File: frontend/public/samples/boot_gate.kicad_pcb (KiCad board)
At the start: 3 parts, among them Q1 2N7002, U1 ATmega328P

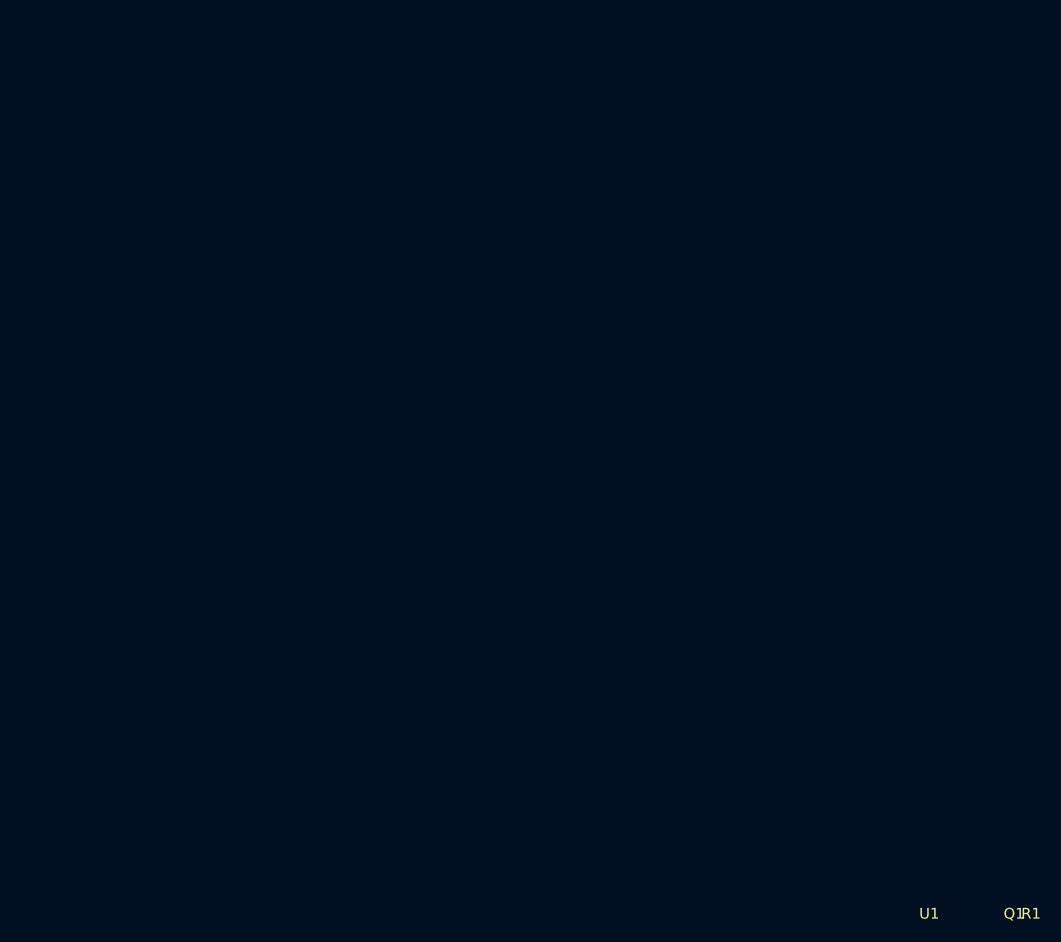
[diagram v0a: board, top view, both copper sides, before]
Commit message: Give the sample boards actual copper
blinky and boot_gate were pad-and-netlist fixtures with zero segments, zero
vias and no board outline, and they are two of the three boards the landing
page offers as one-click samples. A stranger's first click on a tool whose
whole claim is that it starts from the copper produced something that does not
look like a PCB.

Both are routed now, through hauksbee's own board-as-code plus freerouting
path, so repairing the samples exercised a shipped feature end to end. blinky
goes from 0 segments and no outline to 28 segments, an edge, 9 of 9
connections routed and 0 DRC violations. It binds identically: six parts, one
active IC, same verdict.

boot_gate is a judgement rather than a fix. Routing it clean is right for a
sample and wrong for a fixture: waiver_gate.rs asserts it gates red before any
waiver exists, and that premise is the only thing stopping the waiver tests
passing vacuously. Its two shorts come from overlapping pads rather than
traces, so the round-trip drops them. The sample copy is therefore the routed
clean board and the crate fixture keeps its faults, with the samples README
saying so instead of leaving the difference to be discovered.

Separately, the VCD sink failed with a bare "No such file or directory" when
its output path's parent did not exist, naming neither the path nor the
reason, after the simulation had already run. Naming an output under a
directory you have not created yet is an ordinary thing to do. It creates the
parent now. This predates the board change: it fails at HEAD too.
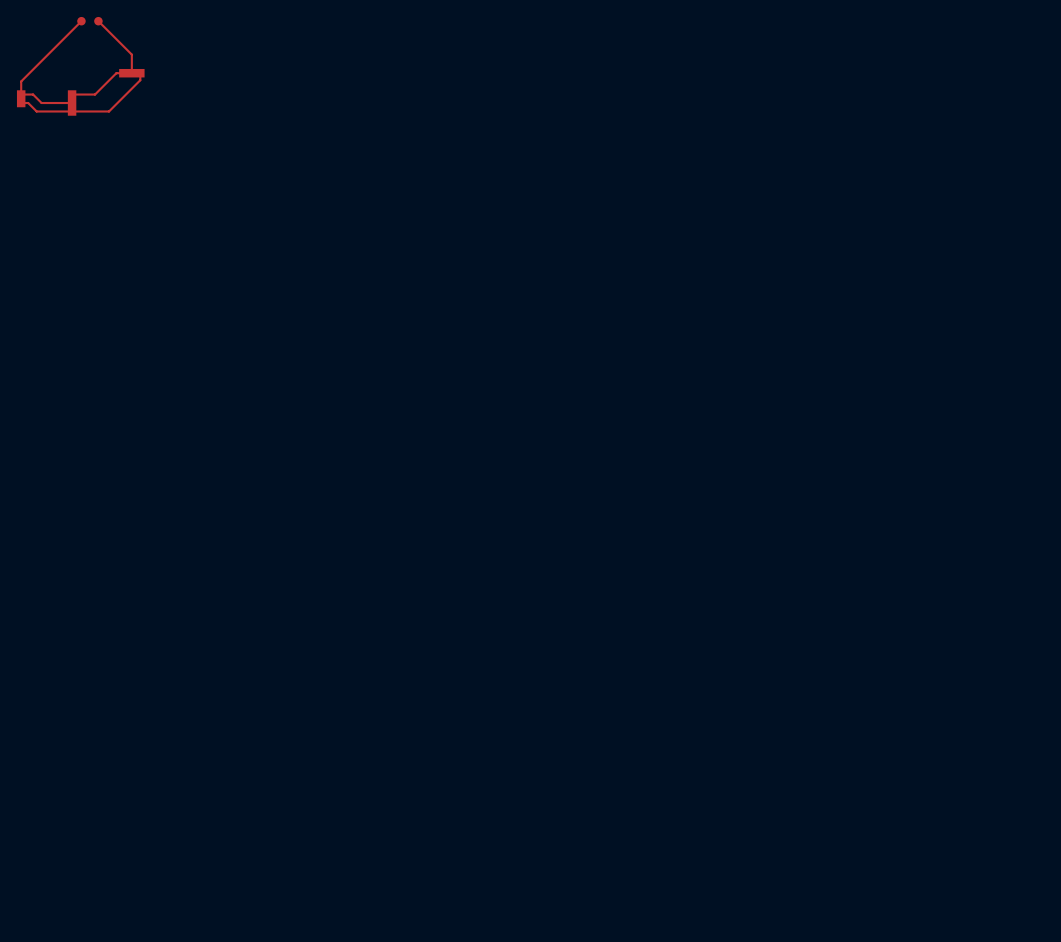
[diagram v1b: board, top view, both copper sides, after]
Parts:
- moved R1 153.7 mm to (0.03, -5.23)
- moved Q1 144.4 mm to (4.97, 0.90)
- moved U1 142.0 mm to (-4.07, 3.42)
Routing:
- net +5V: track 0.00 -> 18.0 mm
- net GND: track 0.00 -> 16.8 mm
- net LOAD_DRAIN: track 0.00 -> 7.77 mm
- net GATE_CTRL: track 0.00 -> 7.09 mm
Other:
- copper layers 0 -> 2
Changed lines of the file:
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@@
-(kicad_pcb (version 20171130) (host pcbnew 5.1.0)
-  (net 0 "")
-  (net 1 "GND")
-  (net 2 "+5V")
-  (net 3 "GATE_CTRL")
-  (net 4 "LOAD_DRAIN")
-  (module Package_QFP:TQFP-32_7x7mm_P0.8mm (layer F.Cu)
-    (at 100 100)
-    (fp_text reference U1 (at 0 0) (layer F.SilkS))
-    (fp_text value ATmega328P (at 0 2) (layer F.Fab))
-    (pad 7  smd rect (at -3 0) (net 2 "+5V"))
-    (pad 8  smd rect (at -3 1) (net 1 "GND"))
-    (pad 14 smd rect (at 3 0) (net 3 "GATE_CTRL"))
-    (pad 20 smd rect (at 3 1) (net 2 "+5V"))
-    (pad 22 smd rect (at 3 2) (net 1 "GND"))
-  )
-  (module Package_TO_SOT_SMD:SOT-23 (layer F.Cu)
-    (at 110 100)
-    (fp_text reference Q1 (at 0 0) (layer F.SilkS))
-    (fp_text value 2N7002 (at 0 2) (layer F.Fab))
-    (pad G smd rect (at 0 0) (net 3 "GATE_CTRL"))
-    (pad D smd rect (at 1 0) (net 4 "LOAD_DRAIN"))
-    (pad S smd rect (at 2 0) (net 1 "GND"))
-  )
-  (module Resistor_THT:R_Axial_DIN0207_L6.3mm_D2.5mm (layer F.Cu)
-    (at 112 100)
-    (fp_text reference R1 (at 0 0) (layer F.SilkS))
-    (fp_text value 1k (at 0 2) (layer F.Fab))
-    (pad 1 thru_hole circle (at 0 0) (net 2 "+5V"))
-    (pad 2 thru_hole circle (at 2 0) (net 4 "LOAD_DRAIN"))
-  )
-)
+(kicad_pcb(version 20171130)(generator "pcbnew")(general(thickness 1.6))(paper "A4")(layers(0 "F.Cu"signal)(31 "B.Cu"signal)(36 "B.SilkS"user)(37 "F.SilkS"user)(38 "B.Mask"user)(39 "F.Mask"user)(44 "Edge.Cuts"user)(48 "B.Fab"user)(49 "F.Fab"user))(setup(pad_to_mask_clearance 0))(net 0 "")(net 1 "+5V")(net 2 "GND")(net 3 "GATE_CTRL")(net 4 "LOAD_DRAIN")(footprint "Package_TO_SOT_SMD:SOT-23"(layer "F.Cu")(at 4.974 0.902 0)(property "Reference""Q1")(property "Value""2N7002")(pad G smd rect(at 0 0 0)(size 1 1)(layers "F.Cu")(net 3 "GATE_CTRL"))(pad D smd rect(at 1 0 0)(size 1 1)(layers "F.Cu")(net 4 "LOAD_DRAIN"))(pad S smd rect(at 2 0 0)(size 1 1)(layers "F.Cu")(net 2 "GND")))(footprint "Package_QFP:TQFP-32_7x7mm_P0.8mm"(layer "F.Cu")(at -4.073 3.415 0)(property "Reference""U1")(property "Value""ATmega328P")(pad 7 smd rect(at -3 0 0)(size 1 1)(layers "F.Cu")(net 1 "+5V"))(pad 8 smd rect(at -3 1 0)(size 1 1)(layers "F.Cu")(net 2 "GND"))(pad 14 smd rect(at 3 0 0)(size 1 1)(layers "F.Cu")(net 3 "GATE_CTRL"))(pad 20 smd rect(at 3 1 0)(size 1 1)(layers "F.Cu")(net 1 "+5V"))(pad 22 smd rect(at 3 2 0)(size 1 1)(layers "F.Cu")(net 2 "GND")))(footprint "Resistor_THT:R_Axial_DIN0207_L6.3mm_D2.5mm"(layer "F.Cu")(at 0.032 -5.231 0)(property "Reference""R1")(property "Value""1k")(pad 1 thru_hole circle(at 0 0 0)(size 1 1)(layers "F.Cu")(net 1 "+5V"))(pad 2 thru_hole circle(at 2 0 0)(size 1 1)(layers "F.Cu")(net 4 "LOAD_DRAIN")))(segment(start -1.073 4.415)(end -4.67 4.415)(width 0.25)(layer "F.Cu")(net 1))(segment(start -4.67 4.415)(end -5.67 3.415)(width 0.25)(layer "F.Cu")(net 1))(segment(start -5.67 3.415)(end -7.073 3.415)(width 0.25)(layer "F.Cu")(net 1))(segment(start 0.032 -5.231)(end -7.073 1.874)(width 0.25)(layer "F.Cu")(net 1))(segment(start -7.073 1.874)(end -7.073 3.415)(width 0.25)(layer "F.Cu")(net 1))(segment(start -1.073 3.415)(end 1.63583 3.415)(width 0.25)(layer "F.Cu")(net 3))(segment(start 1.63583 3.415)(end 4.14883 0.902)(width 0.25)(layer "F.Cu")(net 3))(segment(start 4.974 0.902)(end 4.14883 0.902)(width 0.25)(layer "F.Cu")(net 3))(segment(start -1.073 5.415)(end 3.28617 5.415)(width 0.25)(layer "F.Cu")(net 2))(segment(start 3.28617 5.415)(end 6.974 1.72717)(width 0.25)(layer "F.Cu")(net 2))(segment(start -6.24783 4.415)(end -5.24783 5.415)(width 0.25)(layer "F.Cu")(net 2))(segment(start -5.24783 5.415)(end -1.073 5.415)(width 0.25)(layer "F.Cu")(net 2))(segment(start 6.974 0.902)(end 6.974 1.72717)(width 0.25)(layer "F.Cu")(net 2))(segment(start -7.073 4.415)(end -6.24783 4.415)(width 0.25)(layer "F.Cu")(net 2))(segment(start 2.032 -5.231)(end 5.974 -1.289)(width 0.25)(layer "F.Cu")(net 4))(segment(start 5.974 -1.289)(end 5.974 0.902)(width 0.25)(layer "F.Cu")(net 4)))
